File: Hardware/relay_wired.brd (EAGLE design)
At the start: 100 x 80 mm, 9 parts

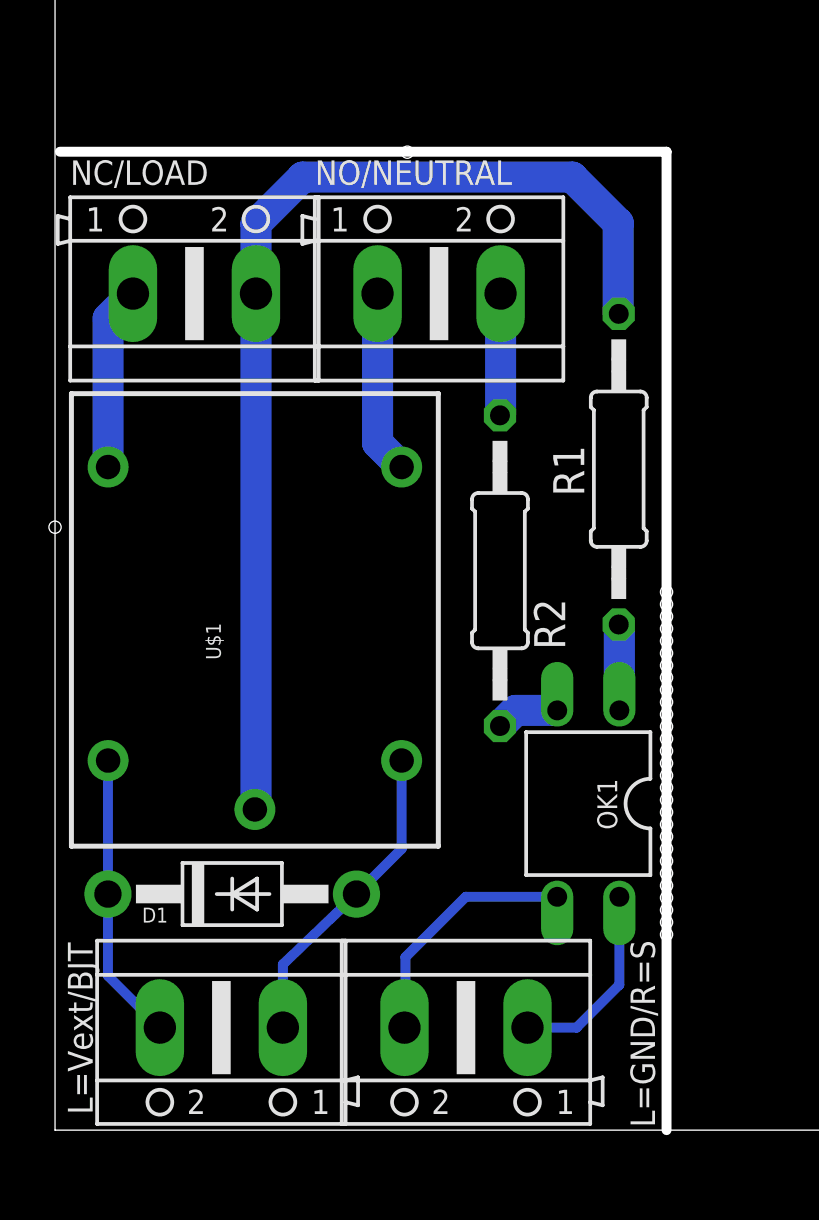
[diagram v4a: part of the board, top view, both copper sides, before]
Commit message: Branching for Omron G5Q-1-EU DC12 relay
- Replaced relay to Omron G5Q-1-EU DC12
- Board size reduced from 40x25 to 32x25
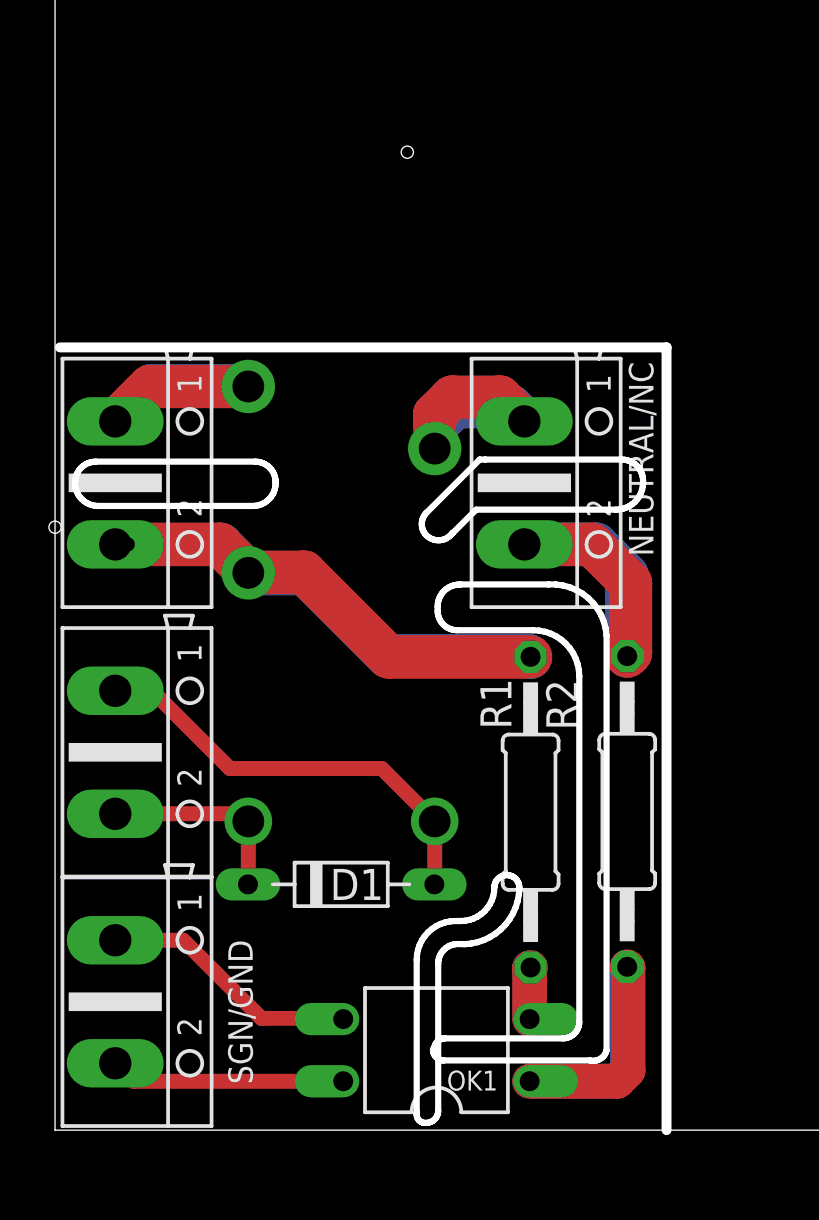
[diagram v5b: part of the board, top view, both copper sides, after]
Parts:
- removed NC/LOAD, NO/NEUTRAL: (no value), con-ptr500:AK500/2
- removed U$1: RELAYPTH, SRD-05VDC-SL-C:SRD-05VDC-SL-C
- added K1: G5Q-1-EU DC12, relay:G5SB
- added LOAD/NO, NEUTRAL/NC: (no value), con-ptr500-modified:AK500/2
- D1: device adafruit:DO41-10 -> diode:D-7.5
- GND/S, VEXT/BJT: device con-ptr500:AK500/2 -> con-ptr500-modified:AK500/2
- moved R1 14.5 mm to (19.4, 13.0)
- moved GND/S 14.4 mm to (2.46, 5.25), turned to 270 degrees
- moved VEXT/BJT 12.1 mm to (2.46, 15.4), turned to 270 degrees
- moved OK1 11.8 mm to (15.6, 3.27), turned to 90 degrees
- moved R2 11.1 mm to (23.4, 13.0)
- moved D1 4.47 mm to (11.7, 10.0)
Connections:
- removed net N$13: D1.A, U$1.COIL0, VEXT/BJT.1
- removed net N$3: NC/LOAD.1, U$1.SWOPEN
- removed net N$5: OK1.2, R2.2
- removed net N$6: OK1.1, R1.2
- new net N$10: GND/S.1, OK1.3
- new net N$14: K1.3, LOAD/NO.1
- new net N$15: K1.4, NEUTRAL/NC.1
- new net N$8: GND/S.2, OK1.4
- net N$1: now also OK1.1, R2.2; no longer D1.C, U$1.COIL1, VEXT/BJT.2
- net N$11: now also D1.C, K1.1, VEXT/BJT.2; no longer GND/S.1, OK1.4
- net N$12: now also D1.A, K1.5, VEXT/BJT.1; no longer GND/S.2, OK1.3
- net N$2: now also OK1.2, R1.2; no longer NO/NEUTRAL.1, U$1.SWCLOSED
- net N$4: now also NEUTRAL/NC.2; no longer NO/NEUTRAL.2
- net N$9: now also K1.2, LOAD/NO.2; no longer NC/LOAD.2, U$1.SWCOMMON
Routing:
- net N$13: track 13.0 -> 0.00 mm
- net N$14: track 0.00 -> 12.1 mm
- net N$4: track 4.99 -> 16.1 mm
- net N$15: track 0.00 -> 10.8 mm
- net N$10: track 0.00 -> 10.7 mm
- net N$8: track 0.00 -> 10.5 mm
- net N$12: track 10.1 -> 17.9 mm
- net N$3: track 7.51 -> 0.00 mm
- net N$9: track 44.1 -> 37.3 mm, vias 0 -> 1
- net N$1: track 11.8 -> 16.8 mm
- net N$6: track 3.52 -> 0.00 mm
- net N$2: track 7.50 -> 4.22 mm
- net N$5: track 2.60 -> 0.00 mm
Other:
- outline, holes or cut-outs redrawn
- board text added: "SGN/GND"
- board text added: "Vext/Bjt"
- board text removed: "L=GND/R=S"
- board text removed: "L=Vext/BJT"

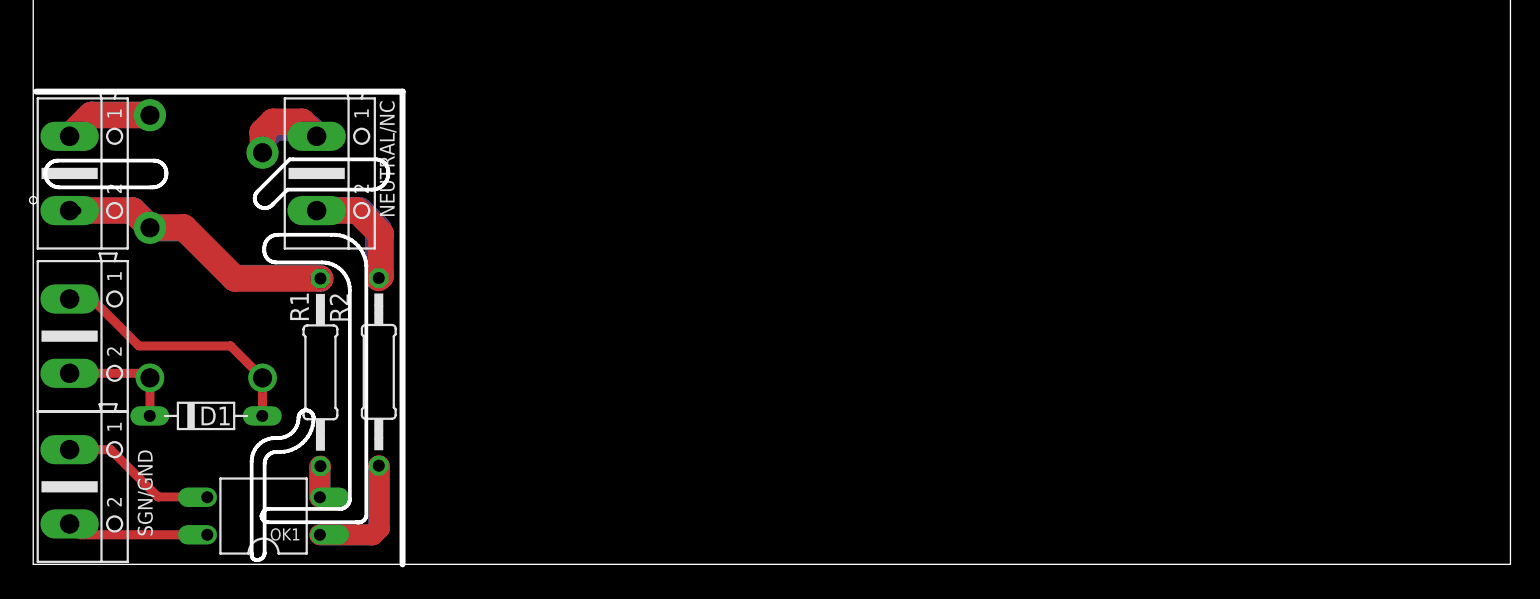
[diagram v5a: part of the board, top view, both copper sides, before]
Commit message: [BUG] Relay was set to mirror by mistake
- A major bug while reviewing where the relay was set to mirror. 
- Updated gerb274x.cam to generate silk screen for bottom also
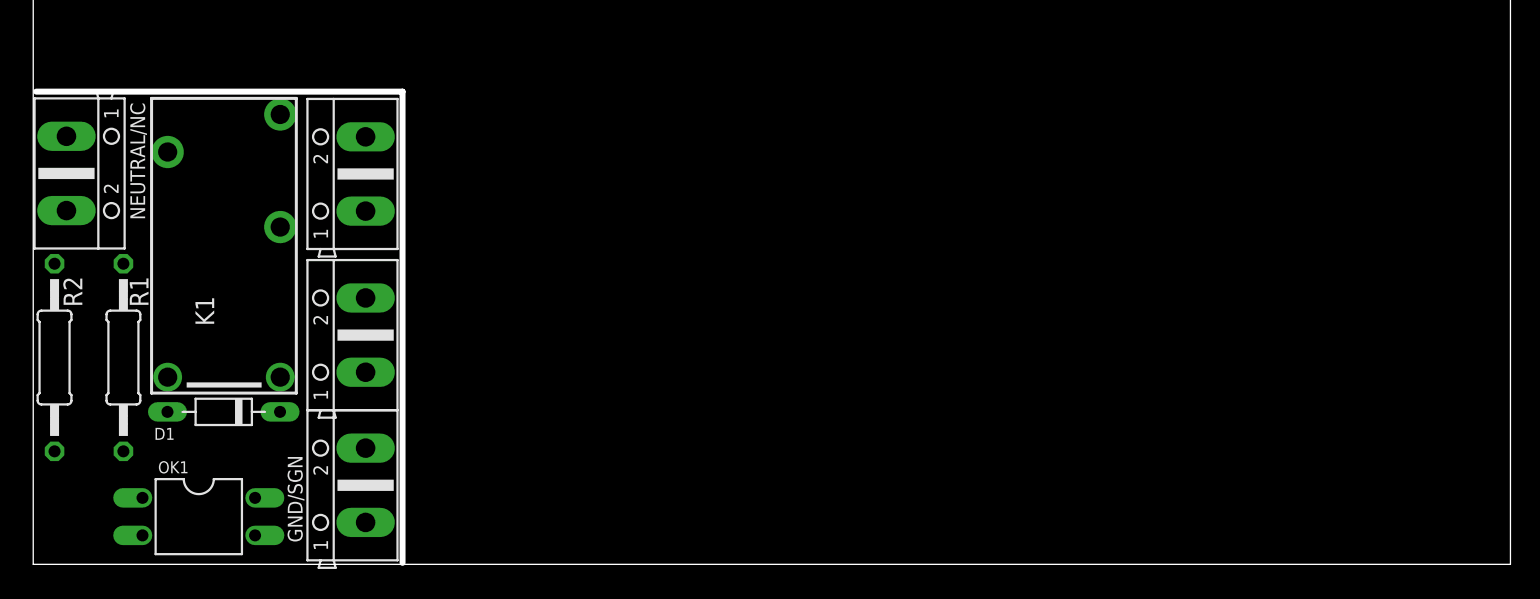
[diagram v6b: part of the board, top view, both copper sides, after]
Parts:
- moved R2 22.0 mm to (1.44, 14.0)
- moved GND/S 20.0 mm to (22.5, 5.35), turned to 90 degrees
- moved VEXT/BJT 20.0 mm to (22.5, 15.5), turned to 90 degrees
- moved LOAD/NO 20.0 mm to (22.5, 26.4), turned to 90 degrees
- moved NEUTRAL/NC 16.9 mm to (2.25, 26.5)
- moved R1 13.4 mm to (6.11, 14.0)
- moved OK1 4.39 mm to (11.2, 3.23), turned to 270 degrees
- moved D1 1.23 mm to (12.9, 10.3), turned to 180 degrees
- moved K1 1.20 mm to (12.9, 20.3), flipped to the top
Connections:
- removed net N$11: D1.C, K1.1, VEXT/BJT.2
- removed net N$12: D1.A, K1.5, VEXT/BJT.1
- removed net N$14: K1.3, LOAD/NO.1
- new net N$6: K1.3, LOAD/NO.2
- new net N$7: D1.C, K1.1, VEXT/BJT.1
- new net N$8: D1.A, K1.5, VEXT/BJT.2
- net N$1: now also OK1.2; no longer OK1.1
- net N$2: now also OK1.1; no longer OK1.2
- net N$9: now also LOAD/NO.1; no longer LOAD/NO.2
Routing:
- net N$9: track 37.3 -> 0.00 mm, vias 1 -> 0
- net N$12: track 17.9 -> 0.00 mm
- net N$1: track 16.8 -> 0.00 mm
- net N$4: track 16.1 -> 0.00 mm
- net N$14: track 12.1 -> 0.00 mm
- net N$15: track 10.8 -> 0.00 mm
- net N$5: track 10.7 -> 0.00 mm
- net N$3: track 10.5 -> 0.00 mm
- net N$11: track 8.15 -> 0.00 mm
- net N$2: track 4.22 -> 0.00 mm
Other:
- outline, holes or cut-outs redrawn
- board text added: "GND/SGN"
- board text removed: "SGN/GND"
- board text removed: "Vext/Bjt"

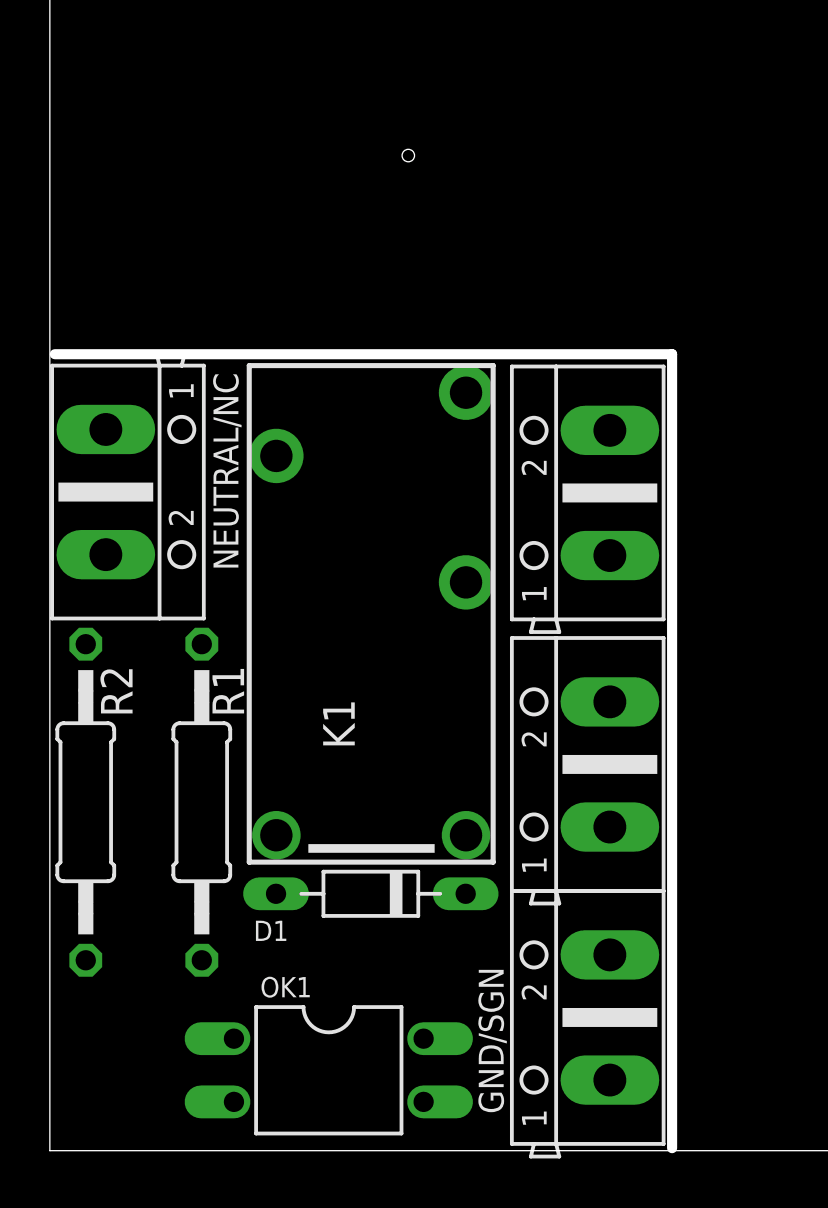
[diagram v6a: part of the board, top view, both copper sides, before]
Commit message: Routing and creepage
- Routed the circuit
- Added creepage as lines not polygon 
- Review is done. Shall be a stable version but not tested yet.
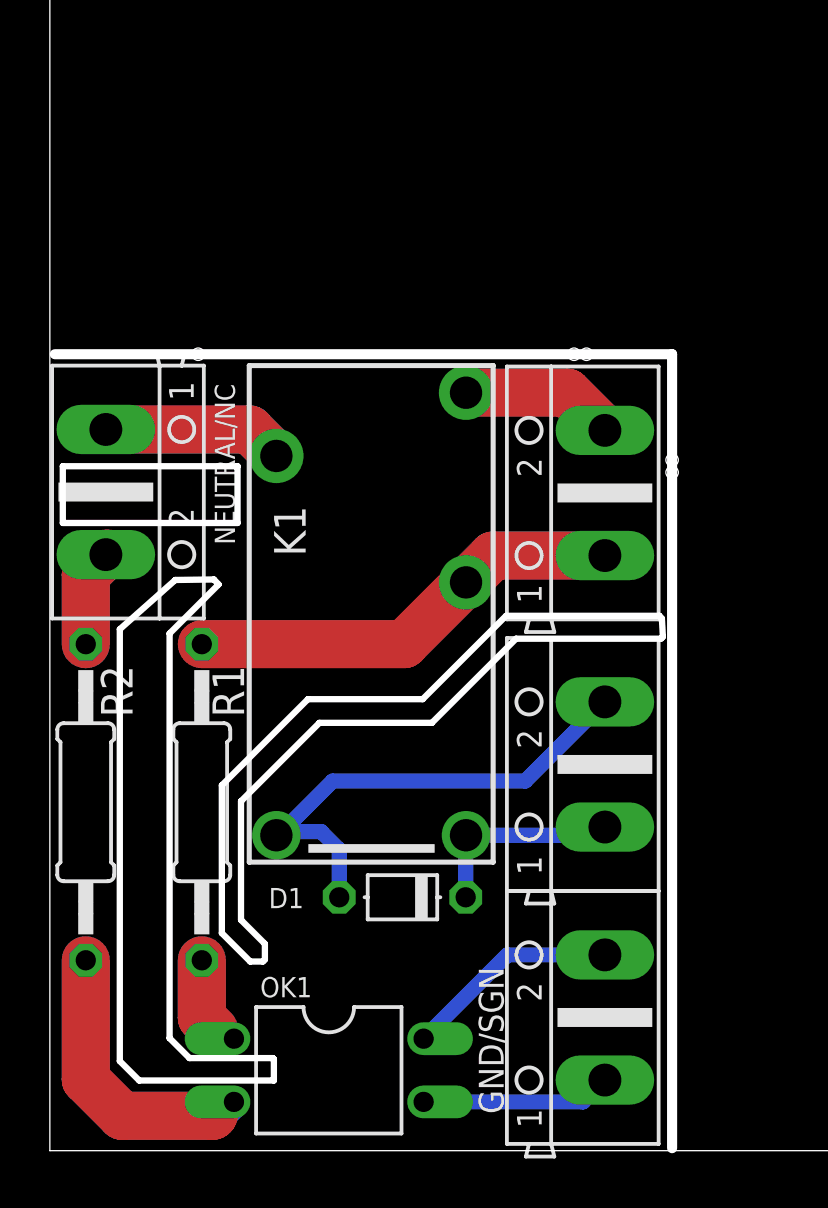
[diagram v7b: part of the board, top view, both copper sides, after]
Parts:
- D1: device diode:D-7.5 -> diode:D-5
- R1, R2: value 22k/1W -> 22k/2W
- moved D1 1.28 mm to (14.2, 10.2)
- moved GND/S 0.20 mm to (22.3, 5.35)
- moved LOAD/NO 0.20 mm to (22.3, 26.4)
- moved VEXT/BJT 0.20 mm to (22.3, 15.5)
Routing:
- net N$9: track 0.00 -> 23.5 mm
- net N$1: track 0.00 -> 23.1 mm
- net N$8: track 0.00 -> 19.8 mm
- net N$15: track 0.00 -> 14.5 mm
- net N$6: track 0.00 -> 12.4 mm
- net N$3: track 0.00 -> 8.68 mm
- net N$7: track 0.00 -> 8.21 mm
- net N$4: track 0.00 -> 7.94 mm
- net N$2: track 0.00 -> 7.90 mm
- net N$5: track 0.00 -> 7.65 mm
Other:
- outline, holes or cut-outs redrawn
